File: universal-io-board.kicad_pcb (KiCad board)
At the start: 2 copper layers, 26 parts, among them J1 Conn_01x03_Pin, J2 Conn_01x22_Socket, J3 Conn_01x22_Socket, U1 R-78E5.0-1.0, U2 AMS1117-3.3, U3 ADS1256IDBT, U4 REF5050IDGK, Y1 Crystal

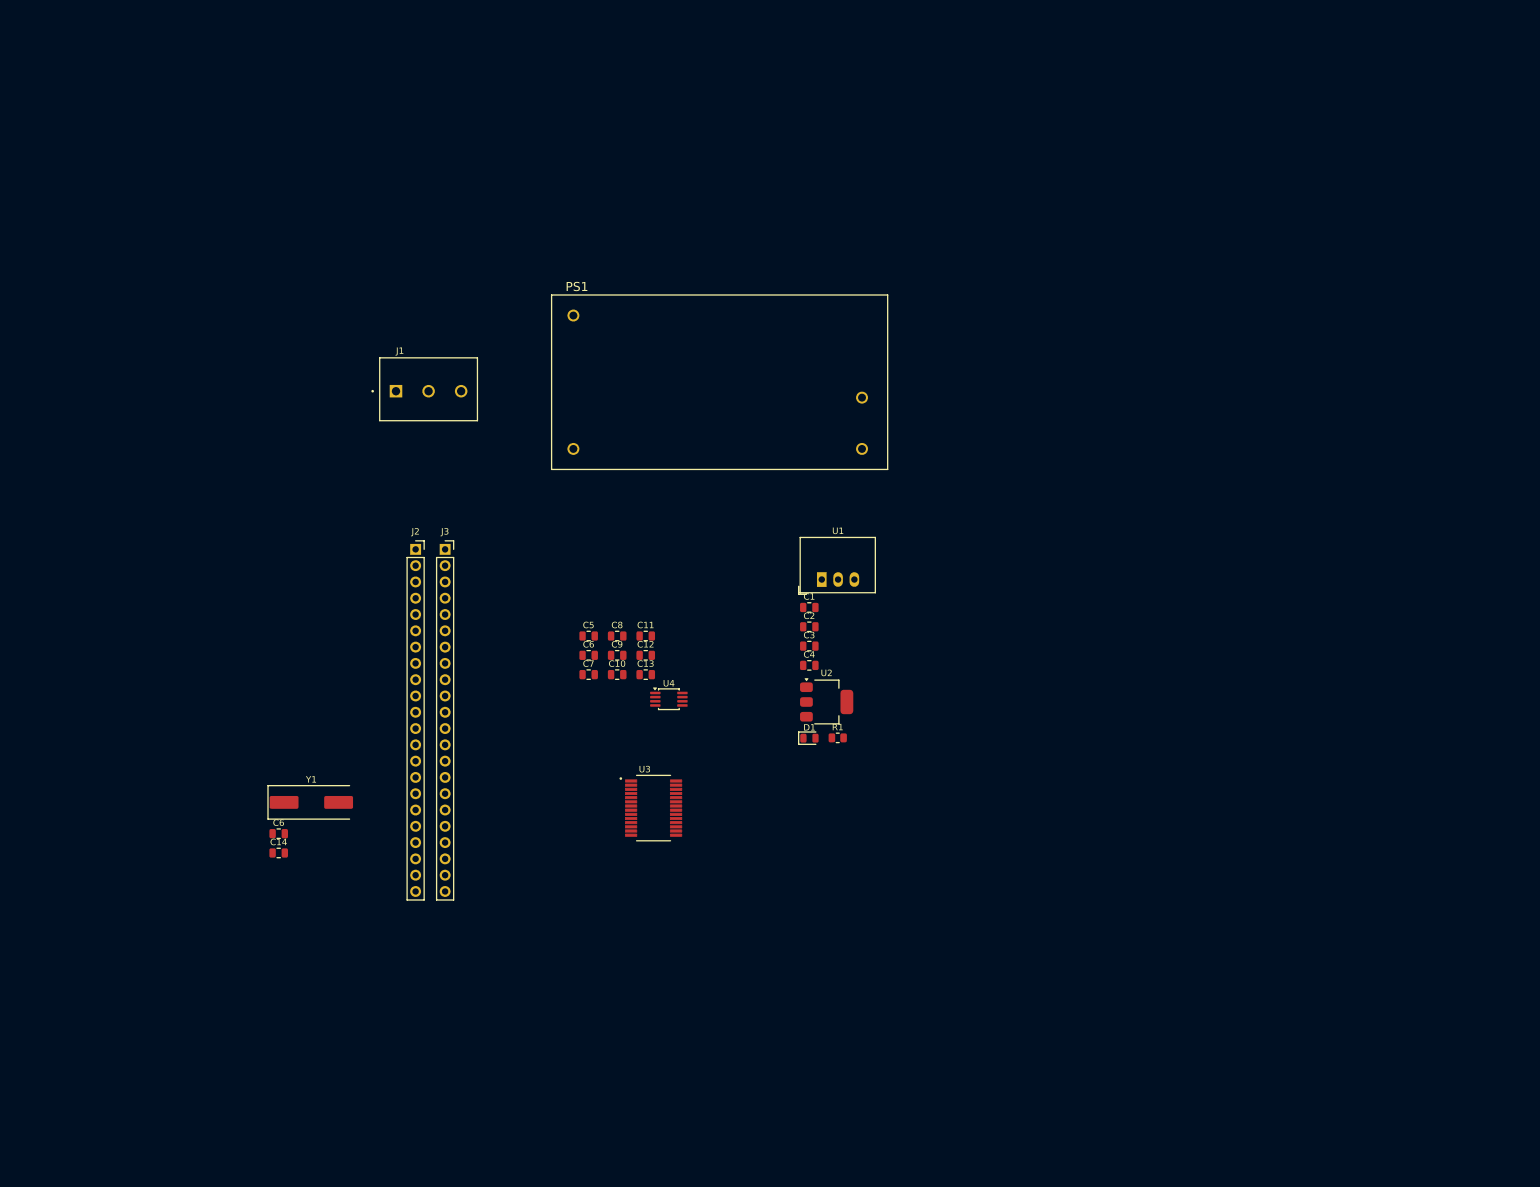
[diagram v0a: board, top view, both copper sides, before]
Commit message: Updated schematic and PCB
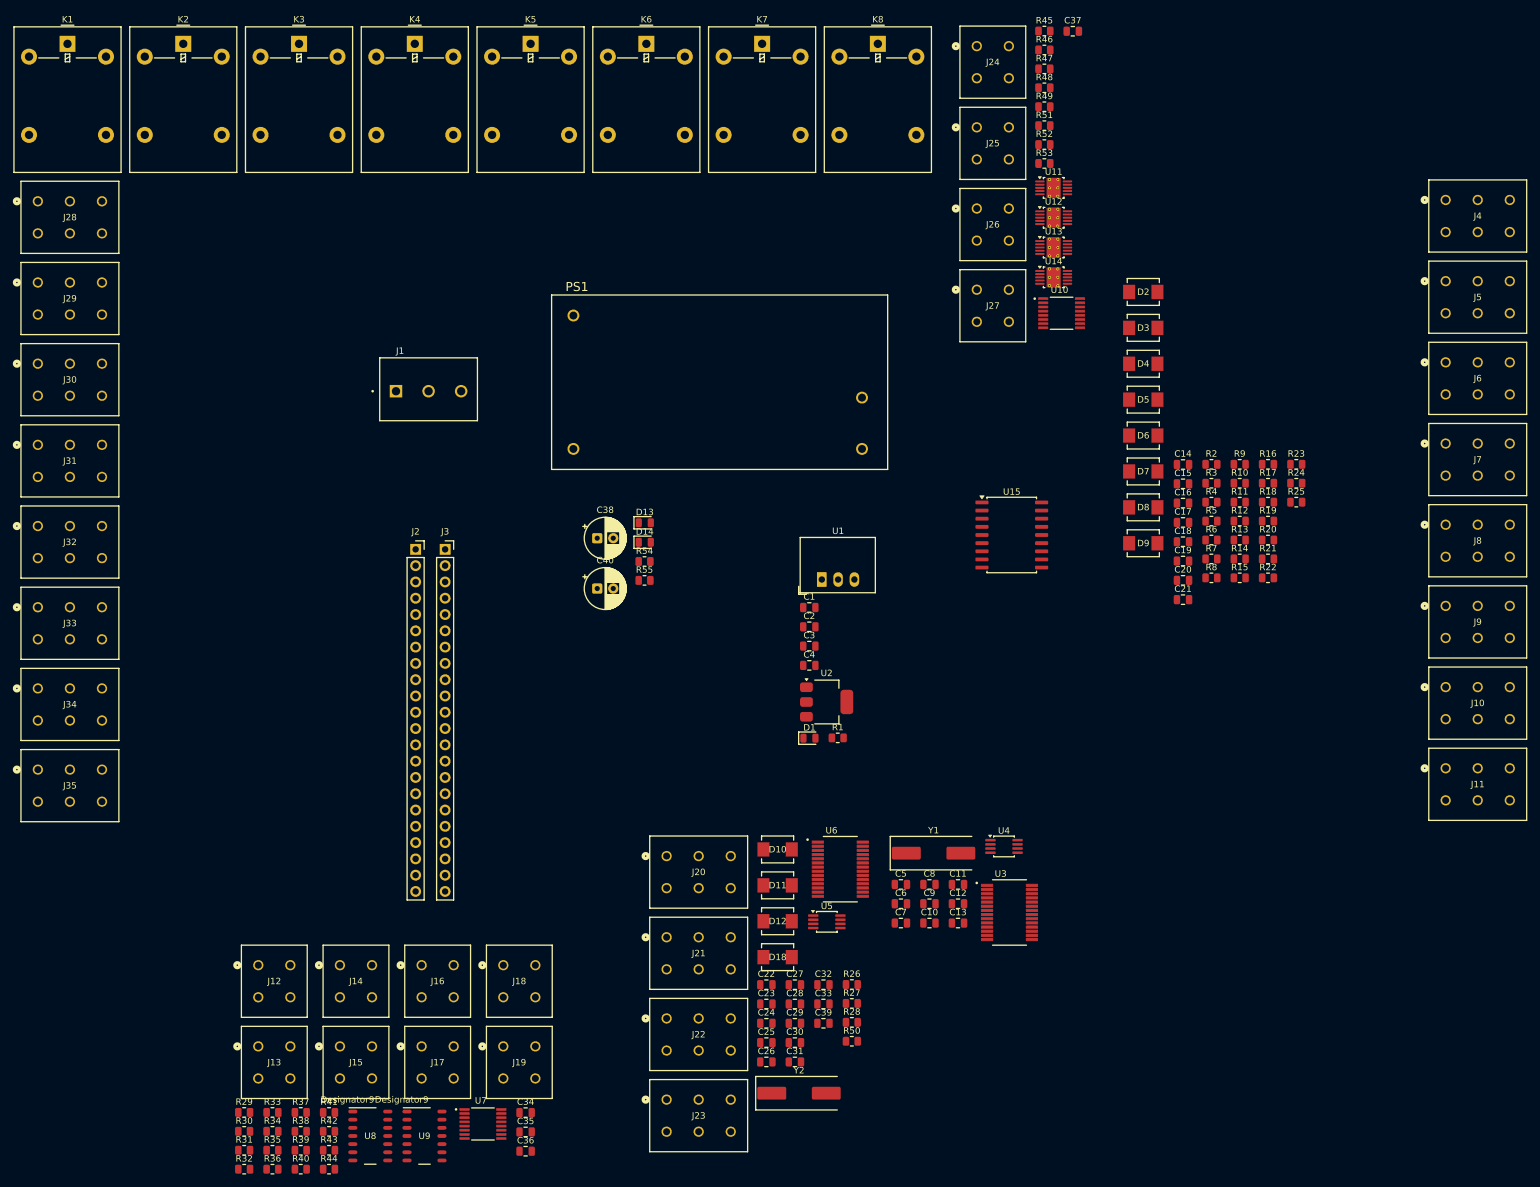
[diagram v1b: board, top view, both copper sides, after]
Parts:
- removed the C6 at (60.0, 135.5)
- removed the C6 at (108.4, 107.7)
- added C15: 100nF, Capacitor_SMD:C_0805_2012Metric, F.Cu at (201.1, 80.9)
- added C16: 100nF, Capacitor_SMD:C_0805_2012Metric, F.Cu at (201.1, 84.0)
- added C17: 100nF, Capacitor_SMD:C_0805_2012Metric, F.Cu at (201.1, 87.0)
- added C18: 100nF, Capacitor_SMD:C_0805_2012Metric, F.Cu at (201.1, 90.0)
- added C19: 100nF, Capacitor_SMD:C_0805_2012Metric, F.Cu at (201.1, 93.0)
- added C20: 100nF, Capacitor_SMD:C_0805_2012Metric, F.Cu at (201.1, 96.0)
- added C21: 100nF, Capacitor_SMD:C_0805_2012Metric, F.Cu at (201.1, 99.0)
- added C22: 100nF, Capacitor_SMD:C_0805_2012Metric, F.Cu at (136.1, 159.0)
- added C23: 1uF, Capacitor_SMD:C_0805_2012Metric, F.Cu at (136.1, 162.0)
- added C24: 10uF, Capacitor_SMD:C_0805_2012Metric, F.Cu at (136.1, 165.1)
- added C25: 18pF, Capacitor_SMD:C_0805_2012Metric, F.Cu at (136.1, 168.1)
- added C26: 18pF, Capacitor_SMD:C_0805_2012Metric, F.Cu at (136.1, 171.1)
- added C27: 10uF, Capacitor_SMD:C_0805_2012Metric, F.Cu at (140.5, 159.0)
- added C28: 100nF, Capacitor_SMD:C_0805_2012Metric, F.Cu at (140.5, 162.0)
- added C29: 10uF, Capacitor_SMD:C_0805_2012Metric, F.Cu at (140.5, 165.1)
- added C30: 100nF, Capacitor_SMD:C_0805_2012Metric, F.Cu at (140.5, 168.1)
- added C31: 100nF, Capacitor_SMD:C_0805_2012Metric, F.Cu at (140.5, 171.1)
- added C32: 100nF, Capacitor_SMD:C_0805_2012Metric, F.Cu at (145.0, 159.0)
- added C33: 100nF, Capacitor_SMD:C_0805_2012Metric, F.Cu at (145.0, 162.0)
- added C34: 2.2uF, Capacitor_SMD:C_0805_2012Metric, F.Cu at (98.5, 179.0)
- added C35: 100nF, Capacitor_SMD:C_0805_2012Metric, F.Cu at (98.5, 182.0)
- added C36: 100nF, Capacitor_SMD:C_0805_2012Metric, F.Cu at (98.5, 185.0)
- added C37: 2.2uF, Capacitor_SMD:C_0805_2012Metric, F.Cu at (183.9, 10.4)
- added C38: 100uF, Capacitor_THT:CP_Radial_D6.3mm_P2.50mm, F.Cu at (109.7, 89.4)
- added C39: 100nF, Capacitor_SMD:C_0805_2012Metric, F.Cu at (145.0, 165.1)
- added C40: 100uF, Capacitor_THT:CP_Radial_D6.3mm_P2.50mm, F.Cu at (109.7, 97.3)
- added C6: 18pF, Capacitor_SMD:C_0805_2012Metric, F.Cu at (157.1, 146.4)
- added D10: D_TVS, footprints:DO-214AASMB_J-BEND_LTF, F.Cu at (137.8, 137.9)
- added D11: D_TVS, footprints:DO-214AASMB_J-BEND_LTF, F.Cu at (137.8, 143.5)
- added D12: D_TVS, footprints:DO-214AASMB_J-BEND_LTF, F.Cu at (137.8, 149.1)
- added D13: LED, LED_SMD:LED_0805_2012Metric, F.Cu at (117.1, 87.0)
- added D14: LED, LED_SMD:LED_0805_2012Metric, F.Cu at (117.1, 90.1)
- added D18: D_TVS, footprints:DO-214AASMB_J-BEND_LTF, F.Cu at (137.8, 154.7)
- added D2: D_TVS, footprints:DO-214AASMB_J-BEND_LTF, F.Cu at (194.9, 51.0)
- added D3: D_TVS, footprints:DO-214AASMB_J-BEND_LTF, F.Cu at (194.9, 56.6)
- added D4: D_TVS, footprints:DO-214AASMB_J-BEND_LTF, F.Cu at (194.9, 62.2)
- added D5: D_TVS, footprints:DO-214AASMB_J-BEND_LTF, F.Cu at (194.9, 67.8)
- added D6: D_TVS, footprints:DO-214AASMB_J-BEND_LTF, F.Cu at (194.9, 73.4)
- added D7: D_TVS, footprints:DO-214AASMB_J-BEND_LTF, F.Cu at (194.9, 79.0)
- added D8: D_TVS, footprints:DO-214AASMB_J-BEND_LTF, F.Cu at (194.9, 84.6)
- added D9: D_TVS, footprints:DO-214AASMB_J-BEND_LTF, F.Cu at (194.9, 90.2)
- added J10: 1862424, SPTAF - External Lever 5.0 mm:CONN_1862424, F.Cu at (252.0, 117.6)
- added J11: 1862424, SPTAF - External Lever 5.0 mm:CONN_1862424, F.Cu at (252.0, 130.3)
- added J12: 1862411, PC Term Block 2 Pos 45deg:CONN_1862411, F.Cu at (61.9, 161.0)
- added J13: 1862411, PC Term Block 2 Pos 45deg:CONN_1862411, F.Cu at (61.9, 173.7)
- added J14: 1862411, PC Term Block 2 Pos 45deg:CONN_1862411, F.Cu at (74.6, 161.0)
- added J15: 1862411, PC Term Block 2 Pos 45deg:CONN_1862411, F.Cu at (74.6, 173.7)
- added J16: 1862411, PC Term Block 2 Pos 45deg:CONN_1862411, F.Cu at (87.3, 161.0)
- added J17: 1862411, PC Term Block 2 Pos 45deg:CONN_1862411, F.Cu at (87.3, 173.7)
- added J18: 1862411, PC Term Block 2 Pos 45deg:CONN_1862411, F.Cu at (100.1, 161.0)
- added J19: 1862411, PC Term Block 2 Pos 45deg:CONN_1862411, F.Cu at (100.1, 173.7)
- added J20: 1862424, SPTAF - External Lever 5.0 mm:CONN_1862424, F.Cu at (130.5, 144.0)
- added J21: 1862424, SPTAF - External Lever 5.0 mm:CONN_1862424, F.Cu at (130.5, 156.6)
- added J22: 1862424, SPTAF - External Lever 5.0 mm:CONN_1862424, F.Cu at (130.5, 169.3)
- added J23: 1862424, SPTAF - External Lever 5.0 mm:CONN_1862424, F.Cu at (130.5, 182.0)
- added J24: 1862411, PC Term Block 2 Pos 45deg:CONN_1862411, F.Cu at (173.9, 17.7)
- added J25: 1862411, PC Term Block 2 Pos 45deg:CONN_1862411, F.Cu at (173.9, 30.4)
- added J26: 1862411, PC Term Block 2 Pos 45deg:CONN_1862411, F.Cu at (173.9, 43.0)
- added J27: 1862411, PC Term Block 2 Pos 45deg:CONN_1862411, F.Cu at (173.9, 55.7)
- added J28: 1862424, SPTAF - External Lever 5.0 mm:CONN_1862424, F.Cu at (32.5, 41.9)
- added J29: 1862424, SPTAF - External Lever 5.0 mm:CONN_1862424, F.Cu at (32.5, 54.5)
- added J30: 1862424, SPTAF - External Lever 5.0 mm:CONN_1862424, F.Cu at (32.5, 67.2)
- added J31: 1862424, SPTAF - External Lever 5.0 mm:CONN_1862424, F.Cu at (32.5, 79.9)
- added J32: 1862424, SPTAF - External Lever 5.0 mm:CONN_1862424, F.Cu at (32.5, 92.5)
- added J33: 1862424, SPTAF - External Lever 5.0 mm:CONN_1862424, F.Cu at (32.5, 105.2)
- added J34: 1862424, SPTAF - External Lever 5.0 mm:CONN_1862424, F.Cu at (32.5, 117.8)
- added J35: 1862424, SPTAF - External Lever 5.0 mm:CONN_1862424, F.Cu at (32.5, 130.5)
- added J4: 1862424, SPTAF - External Lever 5.0 mm:CONN_1862424, F.Cu at (252.0, 41.7)
- added J5: 1862424, SPTAF - External Lever 5.0 mm:CONN_1862424, F.Cu at (252.0, 54.3)
- added J6: 1862424, SPTAF - External Lever 5.0 mm:CONN_1862424, F.Cu at (252.0, 67.0)
- added J7: 1862424, SPTAF - External Lever 5.0 mm:CONN_1862424, F.Cu at (252.0, 79.7)
- added J8: 1862424, SPTAF - External Lever 5.0 mm:CONN_1862424, F.Cu at (252.0, 92.3)
- added J9: 1862424, SPTAF - External Lever 5.0 mm:CONN_1862424, F.Cu at (252.0, 105.0)
- added K1: G5LE-1, Relay_THT:Relay_SPDT_Omron-G5LE-1, F.Cu at (27.1, 12.3)
- added K2: G5LE-1, Relay_THT:Relay_SPDT_Omron-G5LE-1, F.Cu at (45.2, 12.3)
- added K3: G5LE-1, Relay_THT:Relay_SPDT_Omron-G5LE-1, F.Cu at (63.2, 12.3)
- added K4: G5LE-1, Relay_THT:Relay_SPDT_Omron-G5LE-1, F.Cu at (81.3, 12.3)
- added K5: G5LE-1, Relay_THT:Relay_SPDT_Omron-G5LE-1, F.Cu at (99.3, 12.3)
- added K6: G5LE-1, Relay_THT:Relay_SPDT_Omron-G5LE-1, F.Cu at (117.4, 12.3)
- added K7: G5LE-1, Relay_THT:Relay_SPDT_Omron-G5LE-1, F.Cu at (135.4, 12.3)
- added K8: G5LE-1, Relay_THT:Relay_SPDT_Omron-G5LE-1, F.Cu at (153.5, 12.3)
- added R10: 1k, Resistor_SMD:R_0805_2012Metric, F.Cu at (209.9, 80.8)
- added R11: 10k, Resistor_SMD:R_0805_2012Metric, F.Cu at (209.9, 83.8)
- added R12: 10k, Resistor_SMD:R_0805_2012Metric, F.Cu at (209.9, 86.8)
- added R13: 10k, Resistor_SMD:R_0805_2012Metric, F.Cu at (209.9, 89.7)
- added R14: 10k, Resistor_SMD:R_0805_2012Metric, F.Cu at (209.9, 92.7)
- added R15: 10k, Resistor_SMD:R_0805_2012Metric, F.Cu at (209.9, 95.6)
- added R16: 10k, Resistor_SMD:R_0805_2012Metric, F.Cu at (214.3, 77.9)
- added R17: 1k, Resistor_SMD:R_0805_2012Metric, F.Cu at (214.3, 80.8)
- added R18: 1k, Resistor_SMD:R_0805_2012Metric, F.Cu at (214.3, 83.8)
- added R19: 1k, Resistor_SMD:R_0805_2012Metric, F.Cu at (214.3, 86.8)
- added R2: 1k, Resistor_SMD:R_0805_2012Metric, F.Cu at (205.5, 77.9)
- added R20: 10k, Resistor_SMD:R_0805_2012Metric, F.Cu at (214.3, 89.7)
- added R21: 10k, Resistor_SMD:R_0805_2012Metric, F.Cu at (214.3, 92.7)
- added R22: 1k, Resistor_SMD:R_0805_2012Metric, F.Cu at (214.3, 95.6)
- added R23: 10k, Resistor_SMD:R_0805_2012Metric, F.Cu at (218.7, 77.9)
- added R24: 10k, Resistor_SMD:R_0805_2012Metric, F.Cu at (218.7, 80.8)
- added R25: 1k, Resistor_SMD:R_0805_2012Metric, F.Cu at (218.7, 83.8)
- added R26: 249, Resistor_SMD:R_0805_2012Metric, F.Cu at (149.4, 159.0)
- added R27: 249, Resistor_SMD:R_0805_2012Metric, F.Cu at (149.4, 162.0)
- added R28: 249, Resistor_SMD:R_0805_2012Metric, F.Cu at (149.4, 164.9)
- added R29: 10k, Resistor_SMD:R_0805_2012Metric, F.Cu at (54.7, 178.9)
- added R3: 10k, Resistor_SMD:R_0805_2012Metric, F.Cu at (205.5, 80.8)
- added R30: 10k, Resistor_SMD:R_0805_2012Metric, F.Cu at (54.7, 181.9)
- added R31: 10k, Resistor_SMD:R_0805_2012Metric, F.Cu at (54.7, 184.8)
- added R32: 10k, Resistor_SMD:R_0805_2012Metric, F.Cu at (54.7, 187.8)
- added R33: 10k, Resistor_SMD:R_0805_2012Metric, F.Cu at (59.1, 178.9)
- added R34: 10k, Resistor_SMD:R_0805_2012Metric, F.Cu at (59.1, 181.9)
- added R35: 10k, Resistor_SMD:R_0805_2012Metric, F.Cu at (59.1, 184.8)
- added R36: 10k, Resistor_SMD:R_0805_2012Metric, F.Cu at (59.1, 187.8)
- added R37: 10k, Resistor_SMD:R_0805_2012Metric, F.Cu at (63.5, 178.9)
- added R38: 10k, Resistor_SMD:R_0805_2012Metric, F.Cu at (63.5, 181.9)
- added R39: 10k, Resistor_SMD:R_0805_2012Metric, F.Cu at (63.5, 184.8)
- added R4: 10k, Resistor_SMD:R_0805_2012Metric, F.Cu at (205.5, 83.8)
- added R40: 10k, Resistor_SMD:R_0805_2012Metric, F.Cu at (63.5, 187.8)
- added R41: 10k, Resistor_SMD:R_0805_2012Metric, F.Cu at (67.9, 178.9)
- added R42: 10k, Resistor_SMD:R_0805_2012Metric, F.Cu at (67.9, 181.9)
- added R43: 10k, Resistor_SMD:R_0805_2012Metric, F.Cu at (67.9, 184.8)
- added R44: 10k, Resistor_SMD:R_0805_2012Metric, F.Cu at (67.9, 187.8)
- added R45: 100, Resistor_SMD:R_0805_2012Metric, F.Cu at (179.4, 10.3)
- added R46: 20k, Resistor_SMD:R_0805_2012Metric, F.Cu at (179.4, 13.3)
- added R47: 100, Resistor_SMD:R_0805_2012Metric, F.Cu at (179.4, 16.2)
- added R48: 20k, Resistor_SMD:R_0805_2012Metric, F.Cu at (179.4, 19.2)
- added R49: 20k, Resistor_SMD:R_0805_2012Metric, F.Cu at (179.4, 22.1)
- added R5: 10k, Resistor_SMD:R_0805_2012Metric, F.Cu at (205.5, 86.8)
- added R50: 249, Resistor_SMD:R_0805_2012Metric, F.Cu at (149.4, 167.9)
- added R51: 100, Resistor_SMD:R_0805_2012Metric, F.Cu at (179.4, 25.1)
- added R52: 100, Resistor_SMD:R_0805_2012Metric, F.Cu at (179.4, 28.0)
- added R53: 20k, Resistor_SMD:R_0805_2012Metric, F.Cu at (179.4, 31.0)
- added R54: 330, Resistor_SMD:R_0805_2012Metric, F.Cu at (117.1, 93.0)
- added R55: 10k, Resistor_SMD:R_0805_2012Metric, F.Cu at (117.1, 96.0)
- added R6: 10k, Resistor_SMD:R_0805_2012Metric, F.Cu at (205.5, 89.7)
- added R7: 1k, Resistor_SMD:R_0805_2012Metric, F.Cu at (205.5, 92.7)
- added R8: 10k, Resistor_SMD:R_0805_2012Metric, F.Cu at (205.5, 95.6)
- added R9: 10k, Resistor_SMD:R_0805_2012Metric, F.Cu at (209.9, 77.9)
- added U10: DAC8568ICPW, DAC8568ICPW:SOP65P640X120-16N, F.Cu at (182.1, 54.3)
- added U11: XTR111AxDGQ, Package_SO:MSOP-10-1EP_3x3mm_P0.5mm_EP2.2x3.1mm_Mask1.83x1.89mm_ThermalVias, F.Cu at (180.9, 34.8)
- added U12: XTR111AxDGQ, Package_SO:MSOP-10-1EP_3x3mm_P0.5mm_EP2.2x3.1mm_Mask1.83x1.89mm_ThermalVias, F.Cu at (180.9, 39.4)
- added U13: XTR111AxDGQ, Package_SO:MSOP-10-1EP_3x3mm_P0.5mm_EP2.2x3.1mm_Mask1.83x1.89mm_ThermalVias, F.Cu at (180.9, 44.1)
- added U14: XTR111AxDGQ, Package_SO:MSOP-10-1EP_3x3mm_P0.5mm_EP2.2x3.1mm_Mask1.83x1.89mm_ThermalVias, F.Cu at (180.9, 48.7)
- added U15: ULN2803A, Package_SO:SOIC-18W_7.5x11.6mm_P1.27mm, F.Cu at (174.3, 88.9)
- added U5: REF5050IDGK, Package_SO:MSOP-8_3x3mm_P0.65mm, F.Cu at (145.5, 149.2)
- added U6: ADS1256IDBT, ADS1256IDBT:SOP65P780X200-28N, F.Cu at (147.6, 141.0)
- added U7: DAC8568ICPW, DAC8568ICPW:SOP65P640X120-16N, F.Cu at (91.9, 180.8)
- added U8: OPA4192IDR, OP4192:D0014A_N, F.Cu at (74.3, 182.6)
- added U9: OPA4192IDR, OP4192:D0014A_N, F.Cu at (82.8, 182.6)
- added Y2: Crystal, Crystal:Crystal_SMD_HC49-SD, F.Cu at (141.2, 176.0)
- moved C14 153.5 mm to (201.1, 77.9)
- moved Y1 97.3 mm to (162.2, 138.5)
- moved C11 62.2 mm to (166.0, 143.4)
- moved C13 62.2 mm to (166.0, 149.4)
- moved C5 62.2 mm to (157.1, 143.4)
- moved C7 62.2 mm to (157.1, 149.4)
- moved C10 62.2 mm to (161.5, 149.4)
- moved C12 62.2 mm to (166.0, 146.4)
- moved C8 62.2 mm to (161.5, 143.4)
- moved C9 62.2 mm to (161.5, 146.4)
- moved U3 57.8 mm to (174.0, 147.8)
- moved U4 57.1 mm to (173.1, 137.5)
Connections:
- net /VREFP renamed /ADC_0-10V/VREFP
- net /XTAL1/CLKIN renamed /ADC_0-10V/XTAL1/CLKIN
- net /XTAL2 renamed /ADC_0-10V/XTAL2
- C14 pad 1: unconnected-(C14-Pad1) -> GND
- C14 pad 2: unconnected-(C14-Pad2) -> Net-(C14-Pad2)
- J2 pad 10: /GPIO17 -> /ADC2_CS
- J2 pad 11: /GPIO18 -> /ADC2_DRDY
- J2 pad 12: /GPIO8 -> /ADC2_RST
- J2 pad 13: /GPIO3 -> /DAC_CS
- J2 pad 14: /GPIO46 -> /DAC2_CS
- J2 pad 15: /GPIO9 -> /RELAY1
- J2 pad 16: /GPIO10 -> /RELAY2
- J2 pad 17: /GPIO11 -> /RELAY3
- J2 pad 18: /GPIO12 -> /RELAY4
- J2 pad 19: /GPIO13 -> /RELAY5
- J2 pad 20: /GPIO14 -> /RELAY6
- J2 pad 4: /GPIO4 -> /ADC_CS
- J2 pad 5: /GPIO5 -> /SPI_CLK
- J2 pad 6: /GPIO6 -> /SPI_MOSI
- J2 pad 7: /GPIO7 -> /SPI_MISO
- J2 pad 8: /GPIO15 -> /ADC_DRDY
- J2 pad 9: /GPIO16 -> /ADC_RST
- J3 pad 18: /GPIO21 -> /RELAY7
- J3 pad 19: /GPIO20 -> /RELAY8
- R1 pad 1: +3.3V -> +5V
- U3 pad 10: unconnected-(U3-AIN4-Pad10) -> /ADC_0-10V/AIN4
- U3 pad 11: unconnected-(U3-AIN5-Pad11) -> /ADC_0-10V/AIN5
- U3 pad 12: unconnected-(U3-AIN6-Pad12) -> /ADC_0-10V/AIN6
- U3 pad 13: unconnected-(U3-AIN7-Pad13) -> /ADC_0-10V/AIN7
- U3 pad 6: unconnected-(U3-AIN0-Pad6) -> /ADC_0-10V/AIN0
- U3 pad 7: unconnected-(U3-AIN1-Pad7) -> /ADC_0-10V/AIN1
- U3 pad 8: unconnected-(U3-AIN2-Pad8) -> /ADC_0-10V/AIN2
- U3 pad 9: unconnected-(U3-AIN3-Pad9) -> /ADC_0-10V/AIN3

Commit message: Updated schematic and PCB
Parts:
- removed C36: 100nF, Capacitor_SMD:C_0805_2012Metric
- removed C37: 2.2uF, Capacitor_SMD:C_0805_2012Metric
- removed J11, J20, J21, J22, J23, J28, J29, J30, J31, J32, J33, J34, J35, J9: 1862424, SPTAF - External Lever 5.0 mm:CONN_1862424
- removed J12, J13, J14, J15, J16, J17, J18, J19, J24, J25, J26, J27: 1862411, PC Term Block 2 Pos 45deg:CONN_1862411
- removed K5, K6, K7, K8: G5LE-1, Relay_THT:Relay_SPDT_Omron-G5LE-1
- removed R45, R47, R51, R52: 100, Resistor_SMD:R_0805_2012Metric
- removed R46, R48, R49, R53: 20k, Resistor_SMD:R_0805_2012Metric
- removed U10: DAC8568ICPW, DAC8568ICPW:SOP65P640X120-16N
- removed U11, U12: XTR111AxDGQ, Package_SO:MSOP-10-1EP_3x3mm_P0.5mm_EP2.2x3.1mm_Mask1.83x1.89mm_ThermalVias
- added U17: XTR111AxDGQ, Package_SO:MSOP-10-1EP_3x3mm_P0.5mm_EP2.2x3.1mm_Mask1.83x1.89mm_ThermalVias, F.Cu at (131.2, 113.2)
- J1: value Conn_01x03_Pin -> 1757255; footprint 1715734:PHOENIX_1715734 -> MSTBA 2,5 3-G-5,08 - PCB header:1757255
- J10, J4, J5, J6, J8: value 1862424 -> 1190374; footprint SPTAF - External Lever 5.0 mm:CONN_1862424 -> LPTA 2,512-5,0 - PCB terminal block1:PHOENIX_1190374
- J7: value 1862424 -> 1190365; footprint SPTAF - External Lever 5.0 mm:CONN_1862424 -> LPTA 2,5 4-5,0:PHOENIX_1190365
- R37, R38, R41, R42: value 10k -> 100
- R39, R40, R43, R44: value 10k -> 20k
- U9: value OPA4192IDR -> XTR111AxDGQ; footprint OP4192:D0014A_N -> Package_SO:MSOP-10-1EP_3x3mm_P0.5mm_EP2.2x3.1mm_Mask1.83x1.89mm_ThermalVias
- moved J6 209.4 mm to (43.4, 48.9), turned to -90 degrees
- moved J7 204.6 mm to (55.7, 137.4)
- moved J2 183.1 mm to (251.7, 23.7), turned to -90 degrees
- moved J8 178.4 mm to (79.4, 137.4)
- moved J1 167.3 mm to (243.0, 76.3), turned to 90 degrees
- moved R18 148.4 mm to (70.4, 47.5)
- moved R15 146.4 mm to (70.4, 51.0)
- moved R12 139.4 mm to (75.2, 51.0)
- moved K1 137.1 mm to (142.7, 86.2)
- moved K2 137.1 mm to (160.7, 86.2)
- moved K3 137.1 mm to (178.8, 86.2)
- moved K4 137.1 mm to (196.8, 86.2)
- moved J5 136.1 mm to (121.2, 16.5), turned to 180 degrees
- moved R19 135.0 mm to (85.1, 47.5)
- moved C18 132.8 mm to (75.2, 47.5)
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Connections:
- C31 pad 2: /ADC_4-20mA/AIN1 -> /ADC_4-20mA/A1
- C32 pad 2: /ADC_4-20mA/AIN2 -> /ADC_4-20mA/A2
- C33 pad 2: /ADC_4-20mA/AIN3 -> /ADC_4-20mA/A3
- C39 pad 2: /ADC_4-20mA/AIN0 -> /ADC_4-20mA/A0
- D10 pad 1: /ADC_4-20mA/AIN1 -> /ADC_4-20mA/A1
- D11 pad 1: /ADC_4-20mA/AIN2 -> /ADC_4-20mA/A2
- D12 pad 1: /ADC_4-20mA/AIN3 -> /ADC_4-20mA/A3
- D18 pad 1: /ADC_4-20mA/AIN0 -> /ADC_4-20mA/A0
- D2 pad 1: Net-(D2-A1) -> /ADC_0-10V/A0
- D3 pad 1: Net-(D3-A1) -> /ADC_0-10V/A1
- D4 pad 1: Net-(D4-A1) -> /ADC_0-10V/A2
- D5 pad 1: Net-(D5-A1) -> /ADC_0-10V/A3
- D6 pad 1: Net-(D6-A1) -> /ADC_0-10V/A4
- D7 pad 1: Net-(D7-A1) -> /ADC_0-10V/A5
- D8 pad 1: Net-(D8-A1) -> /ADC_0-10V/A6
- D9 pad 1: Net-(D9-A1) -> /ADC_0-10V/A7
- J1 pad 1: /L -> /PE
- J1 pad 3: /PE -> /L
- K1 pad 3: Net-(J28-Pad1) -> Net-(J10-Pad1_1)
- K1 pad 4: Net-(J28-Pad3) -> Net-(J10-Pad2_1)
- K1 pad 5: Net-(J28-Pad5) -> Net-(J10-Pad3_1)
- K2 pad 3: Net-(J29-Pad1) -> Net-(J10-Pad4_1)
- K2 pad 4: Net-(J29-Pad3) -> Net-(J10-Pad5_1)
- K2 pad 5: Net-(J29-Pad5) -> Net-(J10-Pad6_1)
- K3 pad 3: Net-(J30-Pad1) -> Net-(J10-Pad7_1)
- K3 pad 4: Net-(J30-Pad3) -> Net-(J10-Pad8_1)
- K3 pad 5: Net-(J30-Pad5) -> Net-(J10-Pad9_1)
- K4 pad 3: Net-(J31-Pad1) -> Net-(J10-Pad10_1)
- K4 pad 4: Net-(J31-Pad3) -> Net-(J10-Pad11_1)
- K4 pad 5: Net-(J31-Pad5) -> Net-(J10-Pad12_1)
- R10 pad 1: Net-(D4-A1) -> /ADC_0-10V/A2
- R17 pad 1: Net-(D5-A1) -> /ADC_0-10V/A3
- R18 pad 1: Net-(D6-A1) -> /ADC_0-10V/A4
- R19 pad 1: Net-(D7-A1) -> /ADC_0-10V/A5
- R2 pad 1: Net-(D2-A1) -> /ADC_0-10V/A0
- R22 pad 1: Net-(D8-A1) -> /ADC_0-10V/A6
- R25 pad 1: Net-(D9-A1) -> /ADC_0-10V/A7
- R26 pad 2: /ADC_4-20mA/AIN1 -> /ADC_4-20mA/A1
- R27 pad 2: /ADC_4-20mA/AIN2 -> /ADC_4-20mA/A2
- R28 pad 2: /ADC_4-20mA/AIN3 -> /ADC_4-20mA/A3
- R29 pad 1: Net-(U8A-OUT) -> /DAC Outputs (0-10V)/A0
- R31 pad 1: Net-(U8B-OUT) -> /DAC Outputs (0-10V)/A1
- R33 pad 1: Net-(U8C-OUT) -> /DAC Outputs (0-10V)/A2
- R35 pad 1: Net-(U8D-OUT) -> /DAC Outputs (0-10V)/A3
- R37 pad 1: Net-(U9B-OUT) -> GND
- R37 pad 2: Net-(U9B-IN-) -> Net-(U9-REGS)
- R38 pad 1: Net-(U9B-IN-) -> GND
- R38 pad 2: GND -> Net-(U13-REGS)
- R39 pad 1: Net-(U9A-OUT) -> Net-(U9-SET)
- R39 pad 2: Net-(U9A-IN-) -> GND
- R40 pad 1: Net-(U9A-IN-) -> Net-(U13-SET)
- R41 pad 1: Net-(U9D-OUT) -> GND
- R41 pad 2: Net-(U9D-IN-) -> Net-(U14-REGS)
- R42 pad 1: Net-(U9D-IN-) -> GND
- R42 pad 2: GND -> Net-(U17-REGS)
- R43 pad 1: Net-(U9C-OUT) -> Net-(U14-SET)
- R43 pad 2: Net-(U9C-IN-) -> GND
- R44 pad 1: Net-(U9C-IN-) -> Net-(U17-SET)
- R50 pad 2: /ADC_4-20mA/AIN0 -> /ADC_4-20mA/A0
- R7 pad 1: Net-(D3-A1) -> /ADC_0-10V/A1
- U13 pad 2: Net-(U13-IS) -> /DAC Outputs (0-10V)/A5
- U13 pad 6: /DAC Outputs (4-20mA)/AO0 -> /DAC Outputs (0-10V)/AO5
- U14 pad 2: Net-(U14-IS) -> /DAC Outputs (0-10V)/A6
- U14 pad 6: /DAC Outputs (4-20mA)/AO0 -> /DAC Outputs (0-10V)/AO6
- U6 pad 6: /ADC_4-20mA/AIN0 -> /ADC_4-20mA/A0
- U6 pad 7: /ADC_4-20mA/AIN1 -> /ADC_4-20mA/A1
- U6 pad 8: /ADC_4-20mA/AIN2 -> /ADC_4-20mA/A2
- U6 pad 9: /ADC_4-20mA/AIN3 -> /ADC_4-20mA/A3
- U8 pad 1: Net-(U8A-OUT) -> /DAC Outputs (0-10V)/A0
- U8 pad 14: Net-(U8D-OUT) -> /DAC Outputs (0-10V)/A3
- U8 pad 7: Net-(U8B-OUT) -> /DAC Outputs (0-10V)/A1
- U8 pad 8: Net-(U8C-OUT) -> /DAC Outputs (0-10V)/A2
- U9 pad 1: Net-(U9A-OUT) -> +24V
- U9 pad 10: /DAC Outputs (0-10V)/AO6 -> GND
- U9 pad 2: Net-(U9A-IN-) -> /DAC Outputs (0-10V)/A4
- U9 pad 3: /DAC Outputs (0-10V)/AO4 -> Net-(U9-REGS)
- U9 pad 4: +24V -> Net-(U9-REGS)
- U9 pad 5: /DAC Outputs (0-10V)/AO5 -> GND
- U9 pad 6: Net-(U9B-IN-) -> /DAC Outputs (0-10V)/AO4
- U9 pad 7: Net-(U9B-OUT) -> Net-(U9-SET)
- U9 pad 8: Net-(U9C-OUT) -> unconnected-(U9-~{EF}-Pad8)
- U9 pad 9: Net-(U9C-IN-) -> unconnected-(U9-OD-Pad9)
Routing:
- net +24V: track 0.00 -> 627.1 mm, vias 0 -> 5
- net +5V: track 0.00 -> 307.8 mm, vias 0 -> 8
- net +3.3V: track 0.00 -> 285.6 mm, vias 0 -> 5
- net /SPI_MOSI: track 0.00 -> 240.2 mm, vias 0 -> 5
- net /SPI_CLK: track 0.00 -> 237.9 mm, vias 0 -> 3
- net /SPI_MISO: track 0.00 -> 221.7 mm, vias 0 -> 4
- net /DAC Outputs (0-10V)/AO5: track 0.00 -> 213.8 mm, vias 0 -> 2
- net /DAC_CS: track 0.00 -> 203.8 mm, vias 0 -> 3
- net /ADC2_DRDY: track 0.00 -> 192.6 mm, vias 0 -> 1
- net /ADC2_CS: track 0.00 -> 191.9 mm, vias 0 -> 2
- net /ADC2_RST: track 0.00 -> 188.7 mm, vias 0 -> 1
- net /ADC_CS: track 0.00 -> 152.0 mm, vias 0 -> 2
- net /ADC_DRDY: track 0.00 -> 150.2 mm, vias 0 -> 3
- net /ADC_RST: track 0.00 -> 148.4 mm, vias 0 -> 3
- net /RELAY8: track 0.00 -> 94.3 mm, vias 0 -> 2
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- added copper zone on B.Cu, net GND
- added copper zone on F.Cu, net GND
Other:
- board outline added: 211.2 x 122.4 mm
